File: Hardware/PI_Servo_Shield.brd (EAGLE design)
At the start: 65 x 30 mm, 146 parts, among them J1 RASPBERRYPI-40-PIN-GPIO, J19 QWIIC, J20 USB C, J21 Serial, Q1 2N7002PW, Q12 2.5A/30V/105mΩ, Q2 2.5A/30V/105mΩ, Q4 2N7002PW, Q5 2.5A/30V/105mΩ, Q7 2.5A/30V/105mΩ, Q9 2.5A/30V/105mΩ, U1 PCA9685, U2 SN74LVC1G32DCKR, U3 CH340C

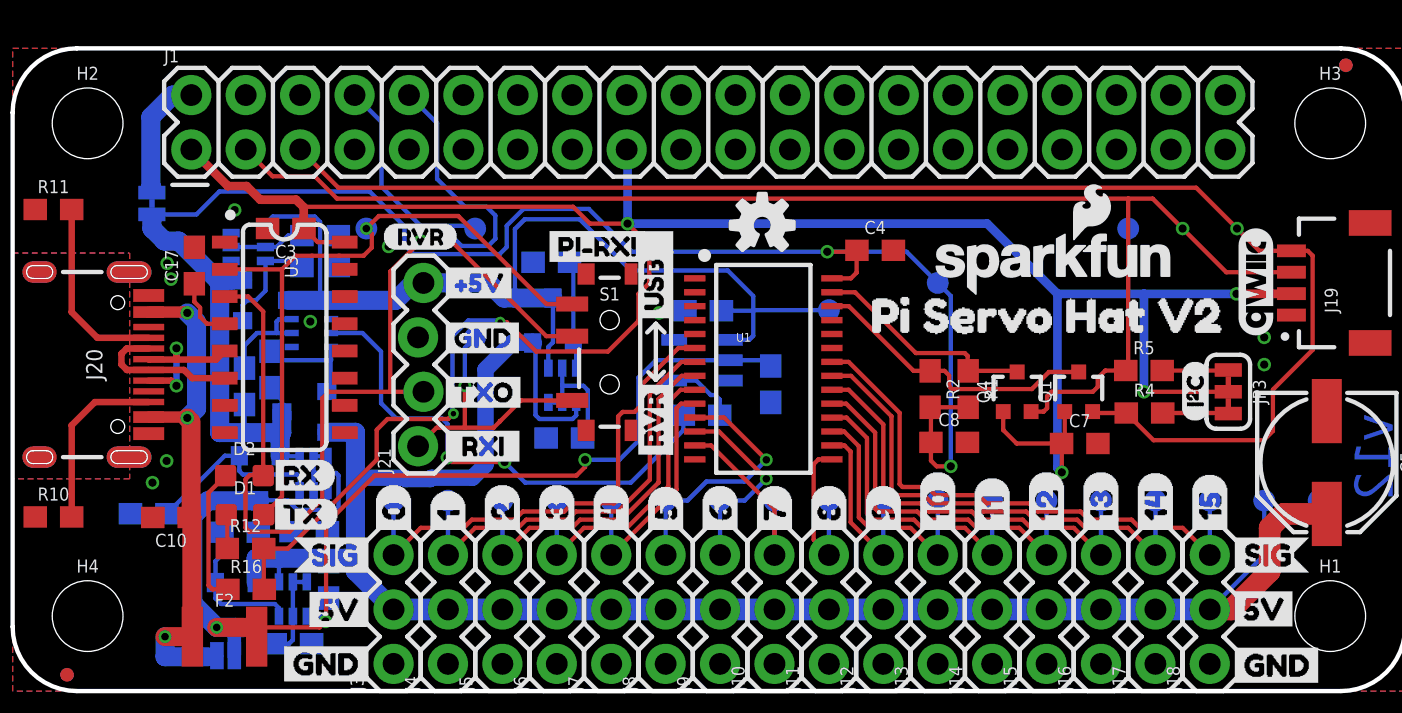
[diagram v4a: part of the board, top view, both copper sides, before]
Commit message: qwiic logo line width and some final minor tweaks
nudged pi iso jumper away to avoid polarity mark on raspi gpio header.
approved DRC errors.
Updated to correct width qwiic logo to avoid long cam jobs
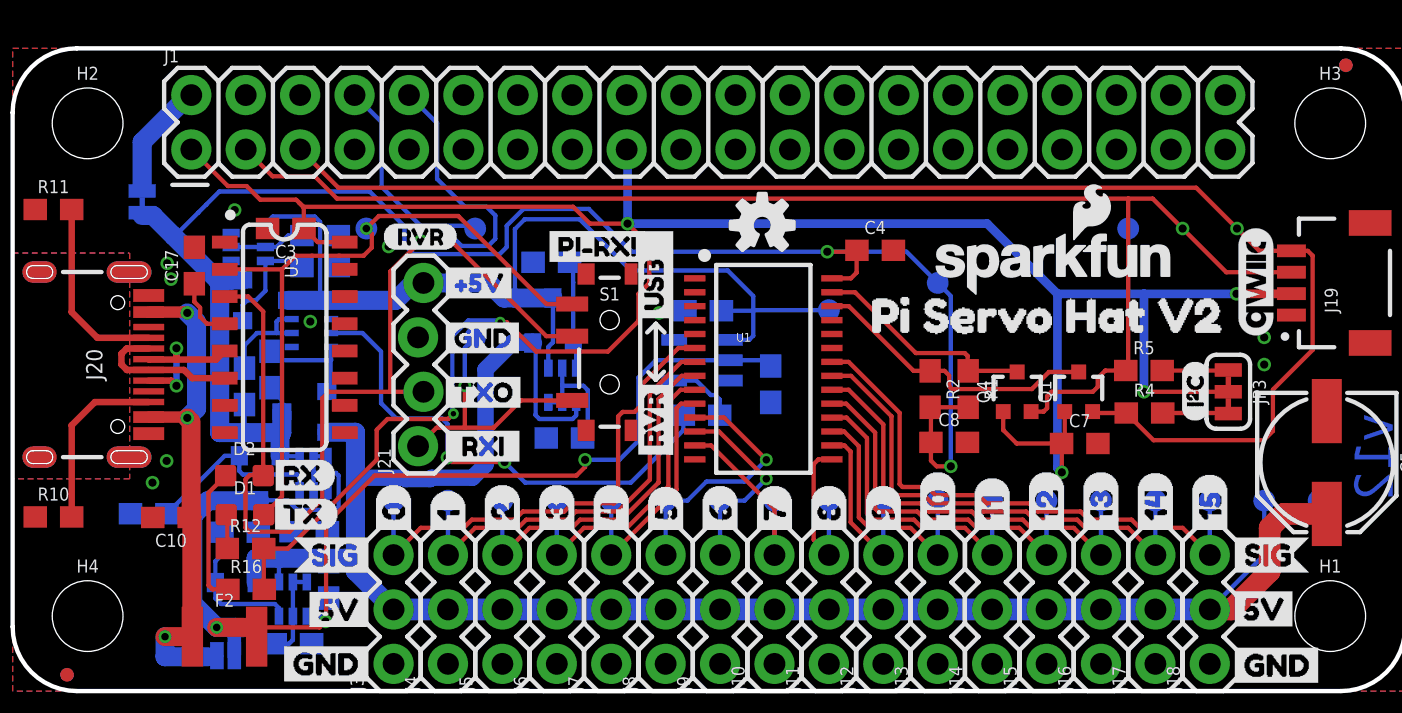
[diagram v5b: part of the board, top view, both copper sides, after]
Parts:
- moved U$32 2.81 mm to (5.49, 22.3), turned to 0 degrees
- moved U$35 2.18 mm to (5.11, 23.4), turned to 0 degrees
- moved JP4 0.46 mm to (6.05, 22.8)
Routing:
- net PI-5V: track 82.5 -> 81.7 mm

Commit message: Corrected package on OR gate
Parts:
- removed U2: SN74LVC1G32DCKR, SparkFun-IC-Logic:SOT23-5
- added U4: 7432SE, SparkFun:SOT353
- moved TP25 1.27 mm to (36.8, 17.8)
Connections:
- net GND: now also U4.3
- net N$17: now also U4.4; no longer U2.4
- net PI-5V: now also U4.5
- net RVR-5V: now also U4.1; no longer U2.1
- net USB-5V: now also U4.2; no longer U2.2
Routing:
- net PI-5V: track 81.7 -> 89.5 mm, vias 2 -> 4
- net LV_SDA: track 65.0 -> 66.2 mm, vias 0 -> 1
- net RVR-5V: track 47.4 -> 48.4 mm

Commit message: Added tRestrict around standofs as required by HAT specs
Also moved to correct 2.5 A PTC (1812 package).
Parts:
- added U$30: (no value), SparkFun-Aesthetics:RASP_μPI_HAT_SPECIFICATION
- F2: value 6V/2A -> 16V/2.5A(5A TRIP); device SparkFun-Fuses:1210 -> SparkFun-Fuses:1812
- moved FD2 6.48 mm to (64.4, 23.1)
- moved FD4 6.48 mm to (64.4, 23.1)
- moved FD1 5.55 mm to (1.52, 6.22)
- moved FD3 5.55 mm to (1.52, 6.22)
- moved R12 3.81 mm to (13.4, 3.84), turned to 270 degrees
- moved R16 1.36 mm to (12.0, 5.56), turned to 270 degrees
- moved F2 1.24 mm to (9.34, 3.65), turned to 270 degrees
- moved D1 0.36 mm to (10.8, 8.59), turned to 180 degrees
- moved U$21 0.30 mm to (13.3, 6.35)
- moved U$37 0.28 mm to (11.8, 8.54)
- moved U$20 0.25 mm to (13.6, 3.81)
- moved D2 0.25 mm to (10.7, 10.3), turned to 180 degrees
- moved U$36 0.22 mm to (11.7, 10.3)
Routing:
- net PI-TXO: track 45.1 -> 36.2 mm
- net 3.3V: track 120.8 -> 124.7 mm
- net USB-5V: track 53.8 -> 50.3 mm, vias 3 -> 4
- net N$7: track 1.60 -> 4.62 mm
- net CH340-TXO: track 31.7 -> 33.6 mm, vias 1 -> 3
- net N$6: track 6.44 -> 4.97 mm
- net VBUS: track 24.0 -> 25.1 mm

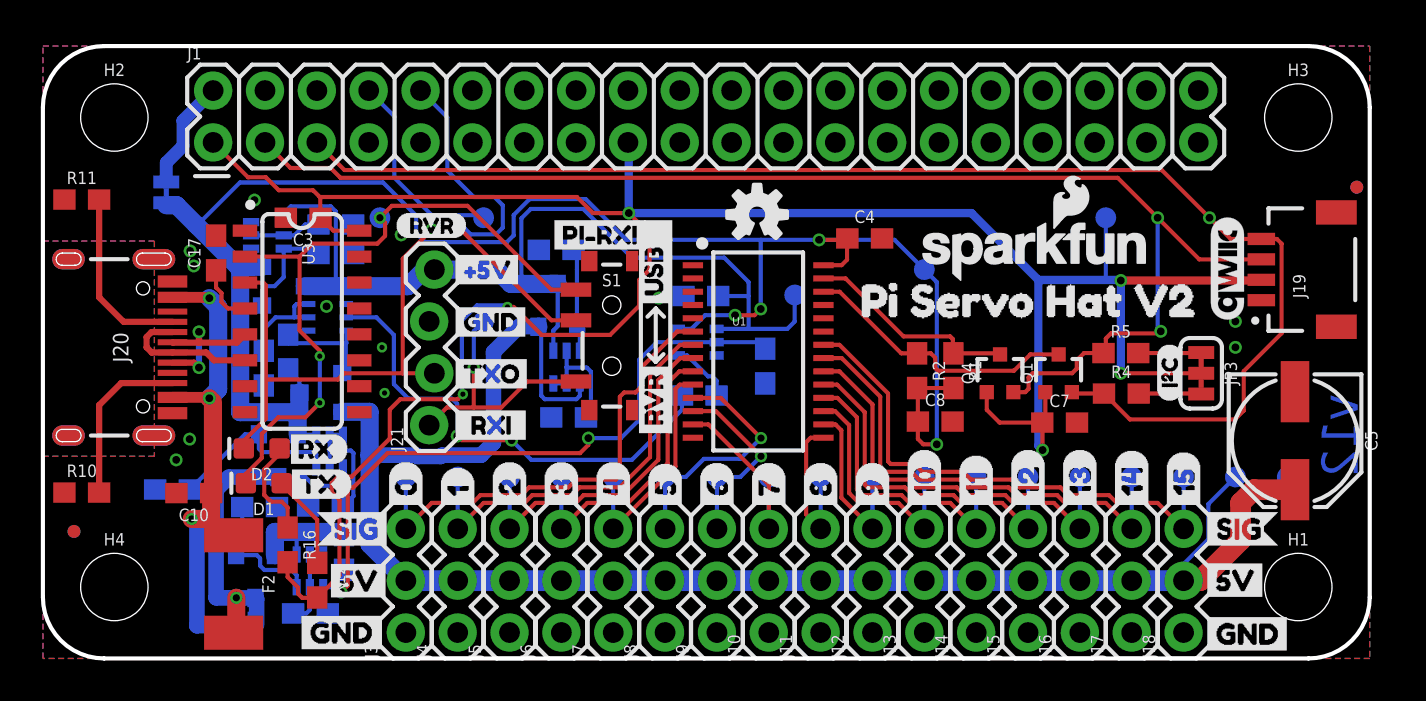
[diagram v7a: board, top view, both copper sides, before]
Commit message: final stuff during eng check for reds
Schematic cleanup.
Corrected OR Gate in latest library to correct SOT353 (was from older library)
Added PROD_ID to dual PNP (TRAN-14386)
moved some vias around to avoid cutting into silk.
re-routed some "natural bridges" on bottom parts.
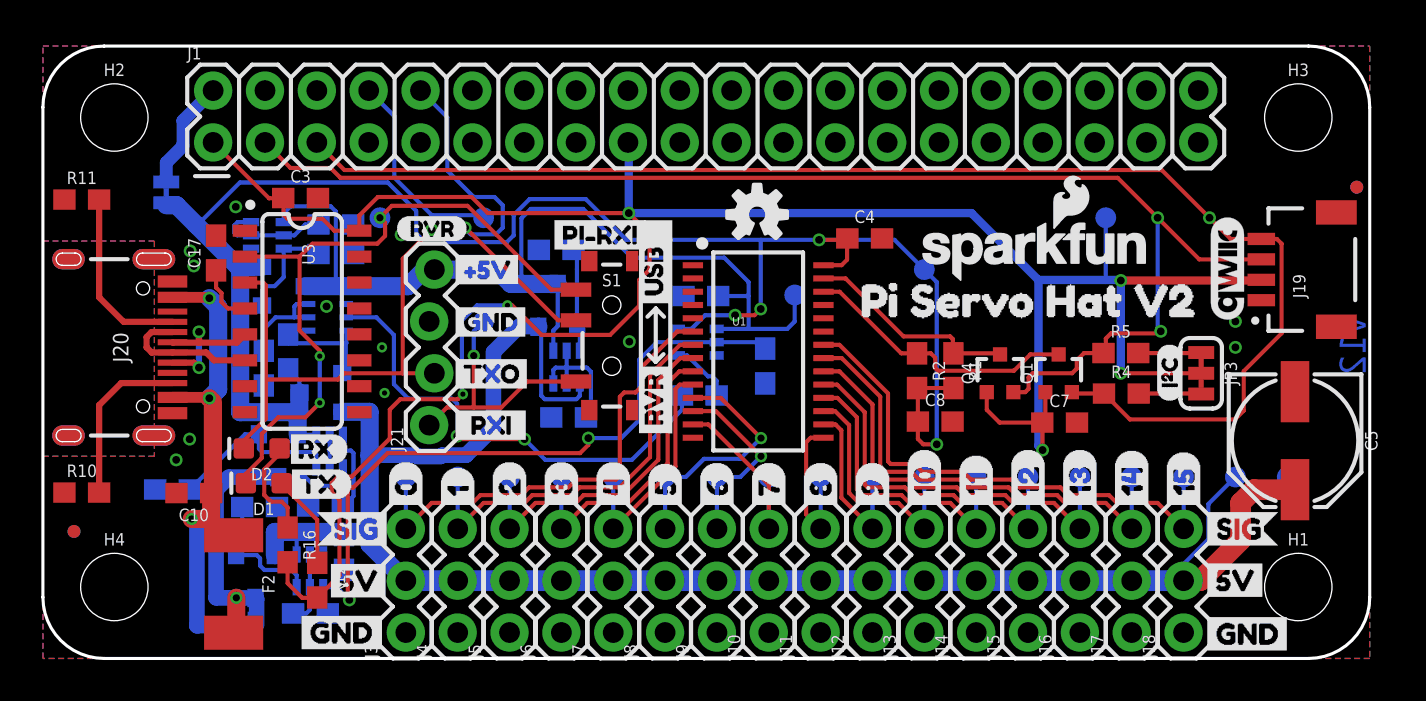
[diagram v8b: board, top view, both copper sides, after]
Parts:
- removed U4: 7432SE, SparkFun:SOT353
- added U2: SN74LVC1G32DCKR, SparkFun-IC-Logic:SOT353
- J21: value Serial -> RVR
- Q1, Q4: value 2N7002PW -> 310mA/60V/1.6Ω
- Q12, Q2, Q5, Q7, Q9: value 2.5A/30V/105mΩ -> 20V/4.2A/52mΩ/1.4W
- R17, R18: value 100 -> 240
- moved C3 0.97 mm to (12.6, 22.6), turned to 0 degrees
- moved U$38 0.15 mm to (17.3, 21.1)
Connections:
- net GND: now also U2.3; no longer U4.3
- net N$17: now also U2.4; no longer U4.4
- net PI-5V: now also U2.5; no longer U4.5
- net RVR-5V: now also U2.1; no longer U4.1
- net USB-5V: now also U2.2; no longer U4.2
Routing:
- net N$16: track 4.17 -> 5.64 mm
- net 3.3V: track 124.7 -> 123.8 mm
- net USB-5V: track 50.3 -> 51.1 mm
- net N$11: track 4.25 -> 5.00 mm
- net N$10: track 5.91 -> 6.64 mm
- net PI-RXI: track 19.0 -> 18.5 mm
